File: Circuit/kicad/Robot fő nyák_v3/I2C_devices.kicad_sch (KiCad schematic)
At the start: 45 parts, among them J19 Conn_01x04_Pin, J20 Conn_01x04_Pin, J21 Conn_01x04_Pin, J23 Conn_01x04_Pin, J24 Conn_01x04_Pin, J25 Conn_01x04_Pin, J26 Conn_01x04_Pin, J27 Conn_01x04_Pin, J28 Conn_01x04_Pin, J29 Conn_01x04_Pin, J30 Conn_01x04_Pin, J31 Conn_01x04_Pin, J32 Conn_01x04_Pin, J33 Conn_01x04_Pin, J34 Conn_01x04_Pin, J35 Conn_01x04_Pin, Q10 IRLML2502, Q11 IRLML2502, Q12 IRLML2502, Q13 IRLML2502, Q14 IRLML2502, Q15 IRLML2502, Q16 IRLML2502, Q17 IRLML2502, Q18 IRLML2502, Q19 IRLML2502, Q4 IRLML2502, Q5 IRLML2502, Q6 IRLML2502, Q7 IRLML2502, Q8 IRLML2502, Q9 IRLML2502, SW2 SW_DIP_x08, U42 TCA9548APWR, U43 TCA9548APWR, U44 74HC240

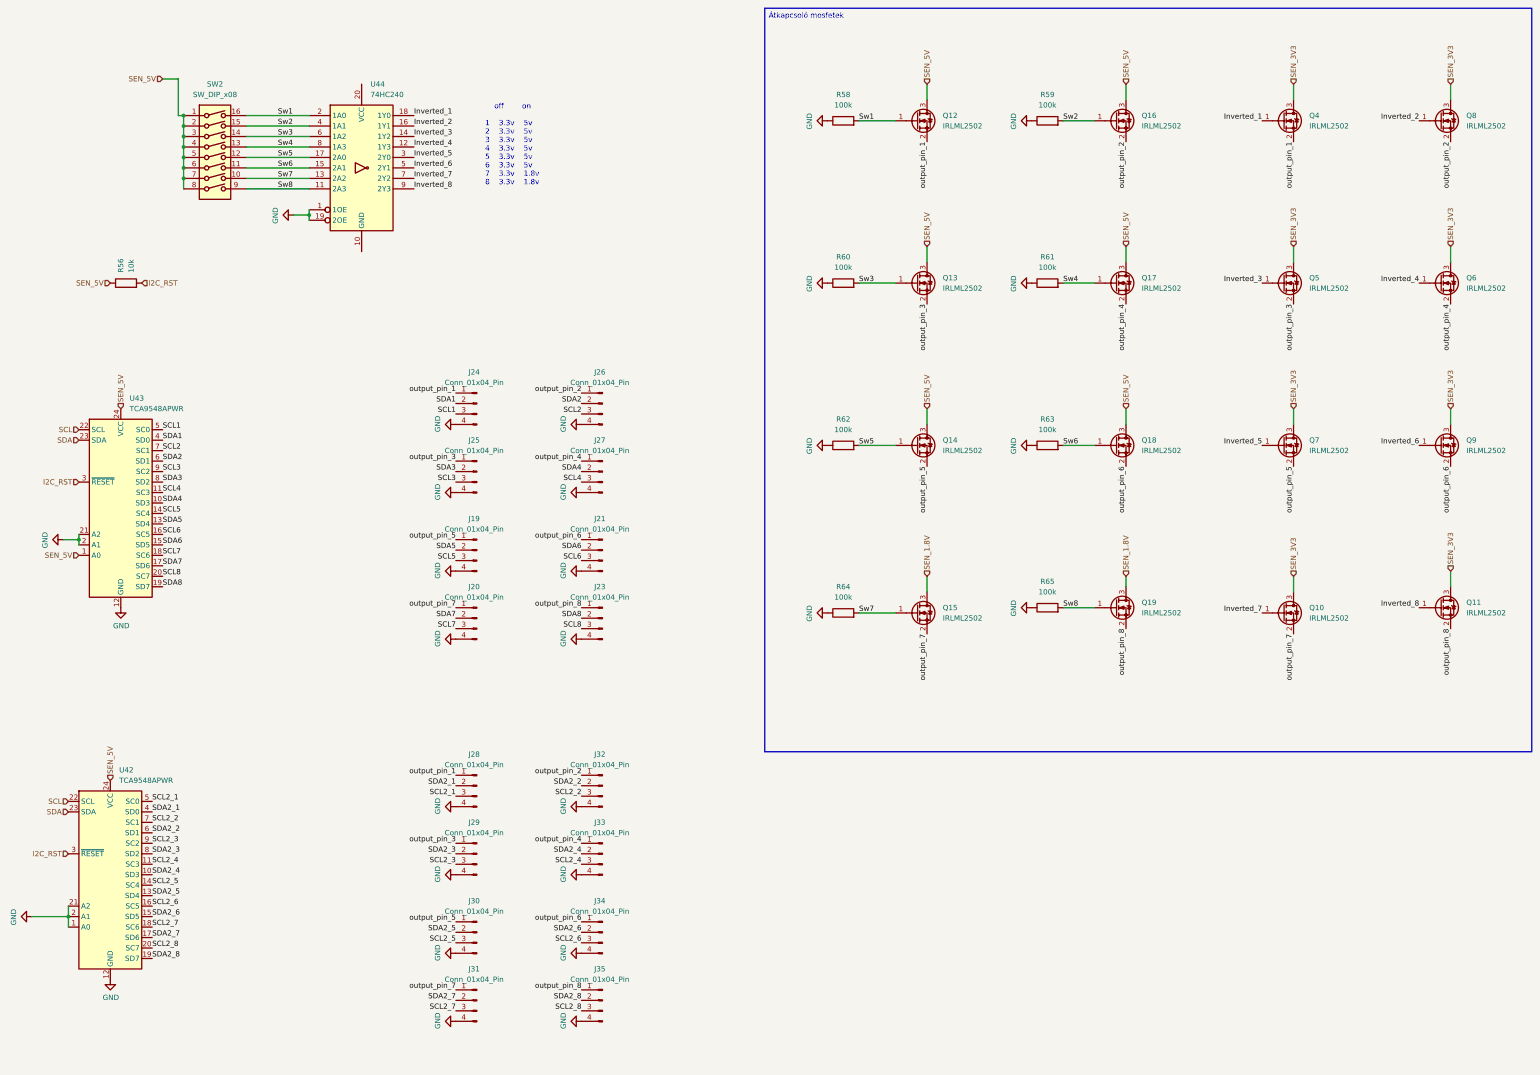
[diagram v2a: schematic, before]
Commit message: kicad v0.1 footprint- assing spi finish
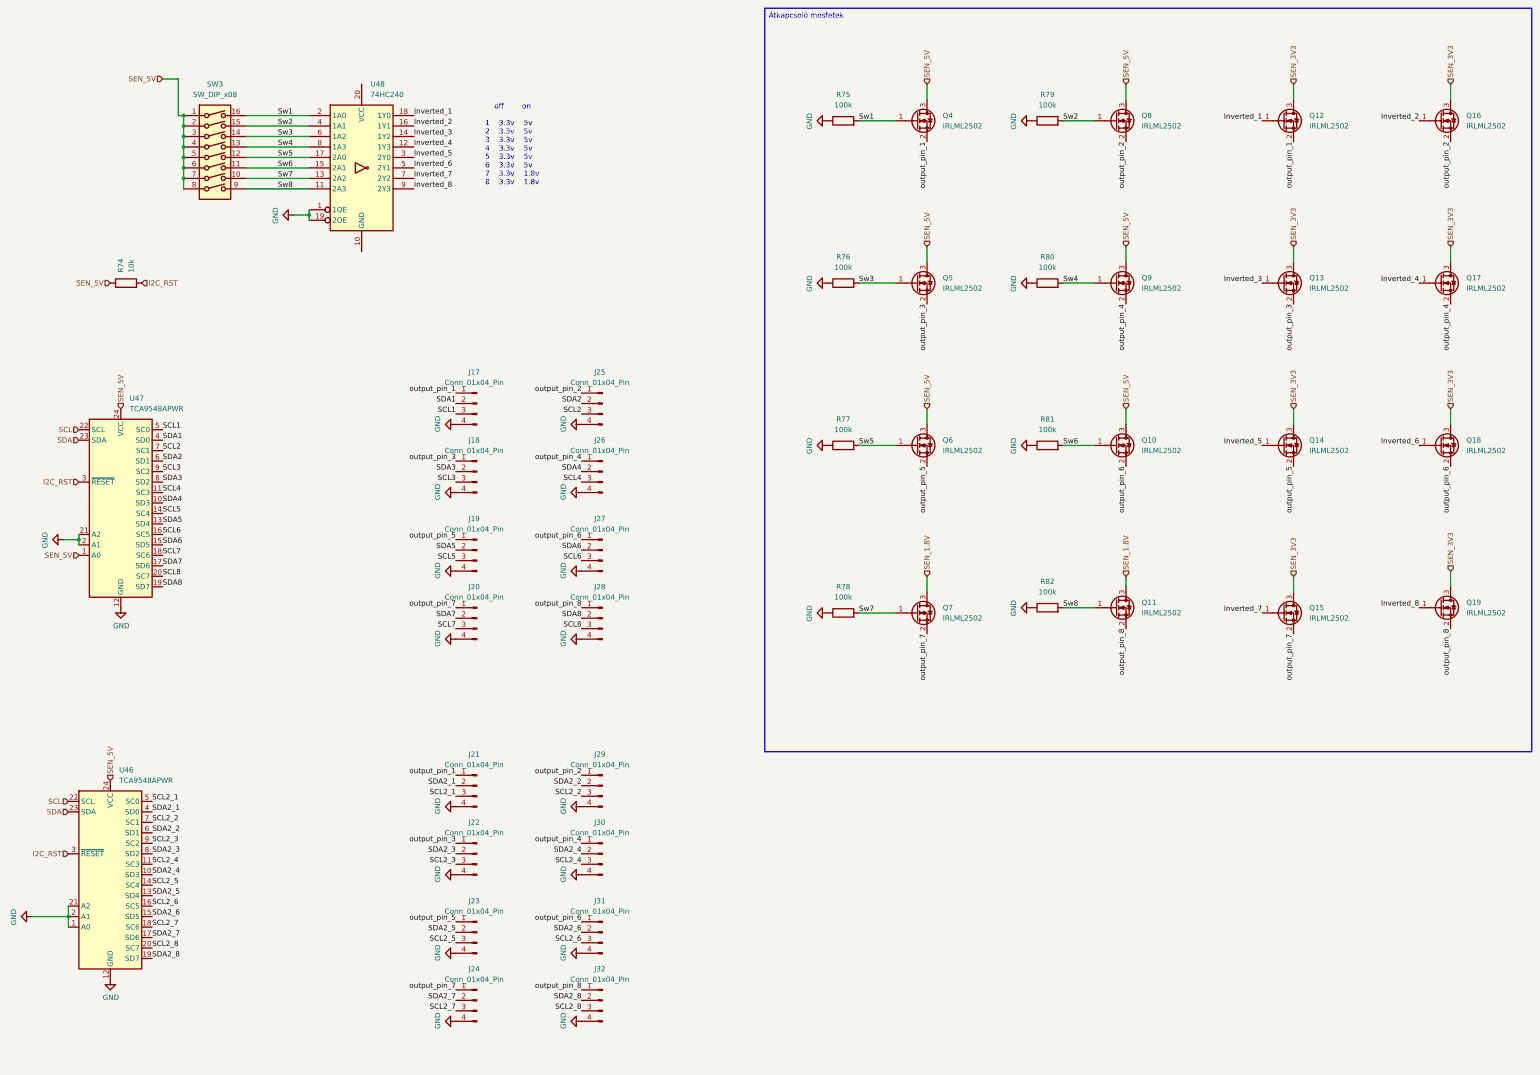
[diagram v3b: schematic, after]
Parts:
- R74: renamed from R56; footprint (none) -> Resistor_SMD:R_0805_2012Metric
- R75: renamed from R58; footprint (none) -> Resistor_SMD:R_0805_2012Metric
- R76: renamed from R60; footprint (none) -> Resistor_SMD:R_0805_2012Metric
- R77: renamed from R62; footprint (none) -> Resistor_SMD:R_0805_2012Metric
- R78: renamed from R64; footprint (none) -> Resistor_SMD:R_0805_2012Metric
- R79: renamed from R59; footprint (none) -> Resistor_SMD:R_0805_2012Metric
- R80: renamed from R61; footprint (none) -> Resistor_SMD:R_0805_2012Metric
- R81: renamed from R63; footprint (none) -> Resistor_SMD:R_0805_2012Metric
- R82: renamed from R65; footprint (none) -> Resistor_SMD:R_0805_2012Metric
- SW3: renamed from SW2; footprint (none) -> Button_Switch_SMD:SW_DIP_SPSTx08_Slide_Copal_CHS-08A_W5.08mm_P1.27mm_JPin
- U48: renamed from U44; footprint (none) -> Package_SO:TSSOP-16_4.4x5mm_P0.65mm
- renumbered J24 to J17, J25 to J18, J28 to J21, J29 to J22, J30 to J23, J31 to J24, J26 to J25, J27 to J26, J21 to J27, J23 to J28, J32 to J29, J33 to J30, J34 to J31, J35 to J32, Q18 to Q10, Q19 to Q11, Q4 to Q12, Q5 to Q13, Q7 to Q14, Q10 to Q15, Q8 to Q16, Q6 to Q17, Q9 to Q18, Q11 to Q19, Q12 to Q4, Q13 to Q5, Q14 to Q6, Q15 to Q7, Q16 to Q8, Q17 to Q9, U42 to U46, U43 to U47

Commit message: kicad update new readme media updates the circuit is 95% finished
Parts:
- added C116, C117, C118: 1uf, Capacitor_SMD:C_0805_2012Metric, symbol Device:C
- added C132, C133, C134, C135, C136, C137, C138, C139: 1uf, symbol Device:C
- added CT5: 10uf, symbol Device:C_Polarized_Small
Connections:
- net GND: now also C116.2, C117.2, C118.2, C132.2, C133.2, C134.2, C135.2, C136.2, C137.2, C138.2, C139.2, CT5.2
- net SEN_5V: now also C116.1, C117.1, C118.1, CT5.1
- net output_pin_1: now also J25.1 (Pin_1), C139.1; no longer J21.1 (Pin_1)
- net output_pin_2: now also J18.1 (Pin_1), J26.1 (Pin_1), C138.1; no longer J25.1 (Pin_1), J29.1 (Pin_1)
- net output_pin_3: now also J19.1 (Pin_1), J27.1 (Pin_1), C137.1; no longer J18.1 (Pin_1), J22.1 (Pin_1)
- net output_pin_4: now also J20.1 (Pin_1), J28.1 (Pin_1), C136.1; no longer J26.1 (Pin_1), J30.1 (Pin_1)
- net output_pin_5: now also J21.1 (Pin_1), J29.1 (Pin_1), C135.1; no longer J19.1 (Pin_1), J23.1 (Pin_1)
- net output_pin_6: now also J22.1 (Pin_1), J30.1 (Pin_1), C134.1; no longer J27.1 (Pin_1), J31.1 (Pin_1)
- net output_pin_7: now also J23.1 (Pin_1), J31.1 (Pin_1), C133.1; no longer J20.1 (Pin_1), J24.1 (Pin_1)
- net output_pin_8: now also J24.1 (Pin_1), C132.1; no longer J28.1 (Pin_1)
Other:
- added sheet PCA9531PW (PCA9531PW.kicad_sch)
- note added: "0x70"
- note added: "0x71"
- note added: "0x72"
- moved on the sheet: R74, U46, U47

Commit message: readme updated kicad circuit V1
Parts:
- added I2C_1, I2C_2: Conn_01x04_Pin, Connector_JST:JST_PH_B4B-PH-K_1x04_P2.00mm_Vertical, symbol Connector:Conn_01x04_Pin
- added R121, R122, R123, R124, R125, R126, R127, R128, R129, R130, R131, R132, R133, R134, R135, R136, R137, R138, R139, R140, R141, R142, R143, R144, R145, R146, R147, R148, R149, R150, R151, R152: 2.2K 1%, Resistor_SMD:R_0805_2012Metric, symbol Device:R
- C85: renamed from C139; footprint (none) -> Capacitor_SMD:C_0805_2012Metric
- C86: renamed from C138; footprint (none) -> Capacitor_SMD:C_0805_2012Metric
- C87: renamed from C137; footprint (none) -> Capacitor_SMD:C_0805_2012Metric
- C88: renamed from C136; footprint (none) -> Capacitor_SMD:C_0805_2012Metric
- C89: renamed from C135; footprint (none) -> Capacitor_SMD:C_0805_2012Metric
- C90: renamed from C134; footprint (none) -> Capacitor_SMD:C_0805_2012Metric
- C91: renamed from C133; footprint (none) -> Capacitor_SMD:C_0805_2012Metric
- C92: renamed from C132; footprint (none) -> Capacitor_SMD:C_0805_2012Metric
- CT4: renamed from CT5; footprint (none) -> Capacitor_Tantalum_SMD:CP_EIA-3528-21_Kemet-B
- U47: renamed from U48; footprint Package_SO:TSSOP-16_4.4x5mm_P0.65mm -> Package_SO:TSSOP-20_4.4x6.5mm_P0.65mm
- renumbered C116 to C93, C117 to C94, C118 to C95, SW3 to DSW3, J21 to I2C_0x70_1, J29 to I2C_0x70_2, J22 to I2C_0x70_3, J30 to I2C_0x70_4, J23 to I2C_0x70_5, J31 to I2C_0x70_6, J24 to I2C_0x70_7, J32 to I2C_0x70_8, J17 to I2C_0x71_1, J25 to I2C_0x71_2, J18 to I2C_0x71_3, J26 to I2C_0x71_4, J19 to I2C_0x71_5, J20 to I2C_0x71_7, J28 to I2C_0x71_8, J27 to JI2C_0x71_6, R74 to R75, R75 to R76, R76 to R77, R77 to R78, R78 to R79, R79 to R80, R80 to R81, R81 to R82, R82 to R83, U47 to U45
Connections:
- net GND: now also I2C_1.4 (Pin_4), I2C_2.4 (Pin_4)
- net SCL: now also I2C_1.3 (Pin_3), I2C_2.3 (Pin_3)
- net SCL1: now also R137.2
- net SCL2: now also R139.2
- net SCL2_1: now also R129.2
- net SCL2_2: now also R131.2
- net SCL2_3: now also R133.2
- net SCL2_4: now also R135.2
- net SCL2_5: now also R125.2
- net SCL2_6: now also R127.2
- net SCL2_7: now also R123.2
- net SCL2_8: now also R122.2
- net SCL3: now also R141.2
- net SCL4: now also R143.2
- net SCL5: now also R145.2
- net SCL6: now also R147.2
- net SCL7: now also R149.2
- net SCL8: now also R151.2
- net SDA: now also I2C_1.2 (Pin_2), I2C_2.2 (Pin_2)
- net SDA1: now also R138.2
- net SDA2: now also R140.2
- net SDA2_1: now also R130.2
- net SDA2_2: now also R132.2
- net SDA2_3: now also R134.2
- net SDA2_4: now also R136.2
- net SDA2_5: now also R126.2
- net SDA2_6: now also R128.2
- net SDA2_7: now also R124.2
- net SDA2_8: now also R121.2
- net SDA3: now also R142.2
- net SDA4: now also R144.2
- net SDA5: now also R146.2
- net SDA6: now also R148.2
- net SDA7: now also R150.2
- net SDA8: now also R152.2
- net SEN_3V3: now also U45.24 (VCC), U46.24 (VCC), I2C_1.1 (Pin_1), I2C_2.1 (Pin_1), R121.1, R122.1, R123.1, R124.1, R125.1, R126.1, R127.1, R128.1, R129.1, R130.1, R131.1, R132.1, R133.1, R134.1, R135.1, R136.1, R137.1, R138.1, R139.1, R140.1, R141.1, R142.1, R143.1, R144.1, R145.1, R146.1, R147.1, R148.1, R149.1, R150.1, R151.1, R152.1
- net SEN_5V: no longer U45.24 (VCC), U46.24 (VCC)
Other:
- moved on the sheet: DSW3, R75, U47
